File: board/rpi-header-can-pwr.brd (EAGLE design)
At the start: 65 x 56.5 mm, 40 parts, among them U1 MCP2515, X1 RJ45-8L21-S, X2 RJ45-8L21-S

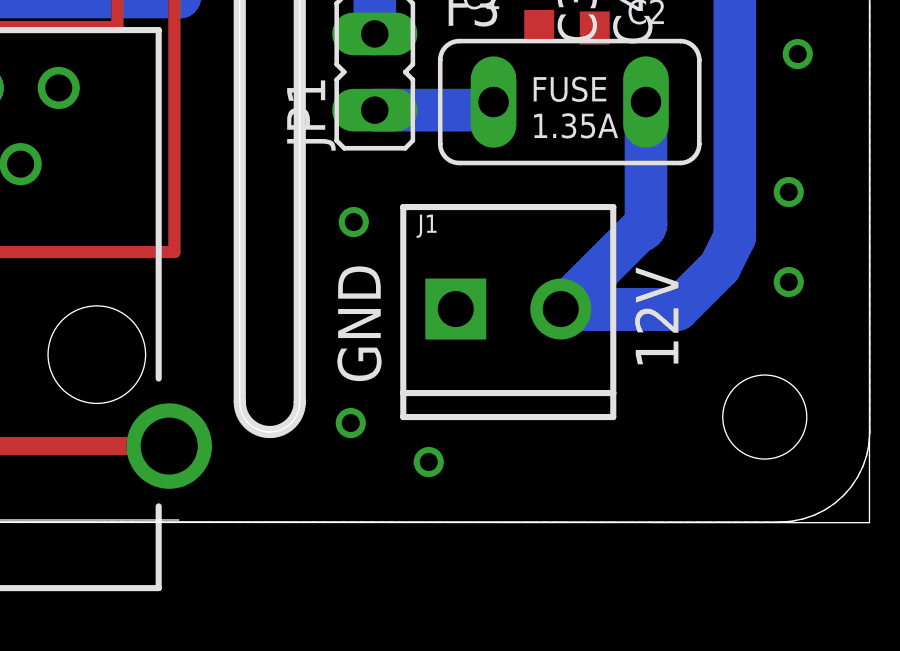
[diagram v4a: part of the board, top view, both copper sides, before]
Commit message: 3.5mm to 5mm screw terminal
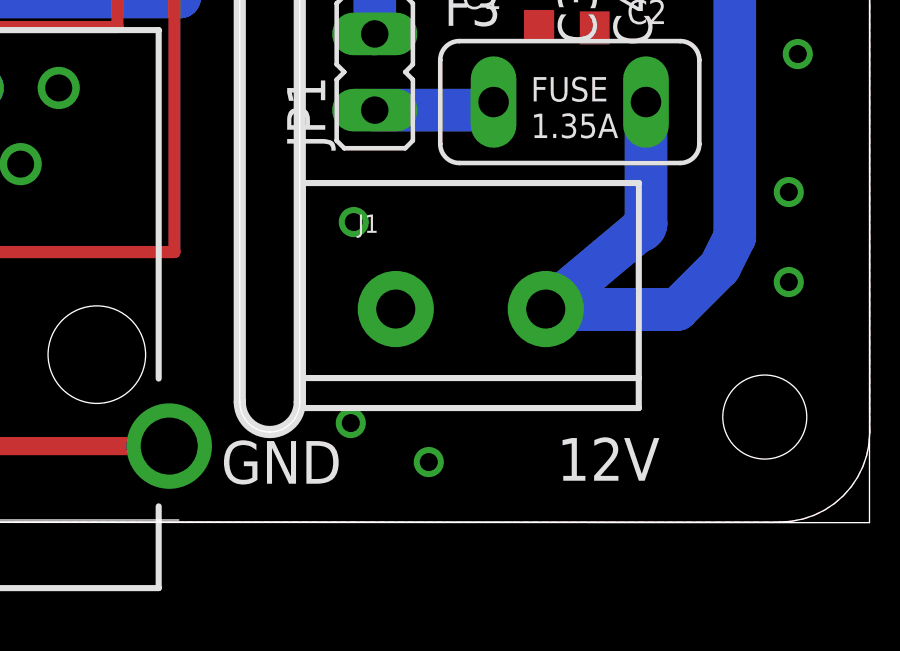
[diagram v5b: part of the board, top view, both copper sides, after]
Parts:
- J1: device SparkFun-Connectors:SCREWTERMINAL-3.5MM-2 -> SparkFun-Connectors:SCREWTERMINAL-5MM-2
- moved J1 2.00 mm to (49.2, 7.10)
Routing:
- net PRE_FUSE_12V: track 42.5 -> 43.4 mm
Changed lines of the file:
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@@
 <text x="6.5" y="43.5" size="1.016" layer="121">FUSE
 2.5A</text>
-<text x="57.2" y="8.5" size="1.4224" layer="121" rot="R270">12V</text>
-<text x="48.7" y="4.6" size="1.4224" layer="121" rot="R90">GND</text>
+<text x="58" y="2.8" size="1.4224" layer="121" rot="R180">12V</text>
+<text x="47.4" y="2.7" size="1.4224" layer="121" rot="R180">GND</text>
 <text x="11.9" y="24.6" size="0.8128" layer="121">D4</text>
 <text x="5.9" y="27.3" size="0.8128" layer="121">R15</text>
@@
 <element name="D3" library="transistor" package="SOT23" value="BC846" x="8" y="38" rot="MR0"/>
 <element name="R4" library="rcl" package="R0603" value="1k" x="8" y="33" rot="MR270"/>
-<element name="J1" library="SparkFun-Connectors" package="SCREWTERMINAL-3.5MM-2" value="" x="51.2" y="7.1">
-<attribute name="PROD_ID" value="CONN-08399" x="51.2" y="7.1" size="1.778" layer="27" display="off"/>
+<element name="J1" library="SparkFun-Connectors" package="SCREWTERMINAL-5MM-2" value="" x="49.2" y="7.1">
+<attribute name="SF_SKU" value="PRT-08432" x="49.2" y="7.1" size="1.778" layer="27" display="off"/>
 </element>
 <element name="GND84" library="SparkFun-Connectors" package="SCREWTERMINAL-3.5MM-2" value="" x="4.5" y="15.5" rot="R270">
@@
 <contactref element="F3" pad="2"/>
 <contactref element="J1" pad="2"/>
-<wire x1="54.7" y1="7.1" x2="54.7" y2="7.085796875" width="1.4224" layer="16"/>
+<wire x1="54.2" y1="7.1" x2="54.7" y2="7.085796875" width="1.4224" layer="16"/>
 <wire x1="57.54" y1="9.94" x2="57.3" y2="9.7" width="1.4224" layer="16"/>
-<wire x1="57.3" y1="9.7" x2="54.7" y2="7.1" width="1.4224" layer="16"/>
+<wire x1="57.3" y1="9.7" x2="54.2" y2="7.1" width="1.4224" layer="16"/>
 <wire x1="54.7" y1="7.085796875" x2="58.585796875" y2="7.085796875" width="1.4224" layer="16"/>
 <wire x1="58.585796875" y1="7.085796875" x2="60" y2="8.5" width="1.4224" layer="16"/>

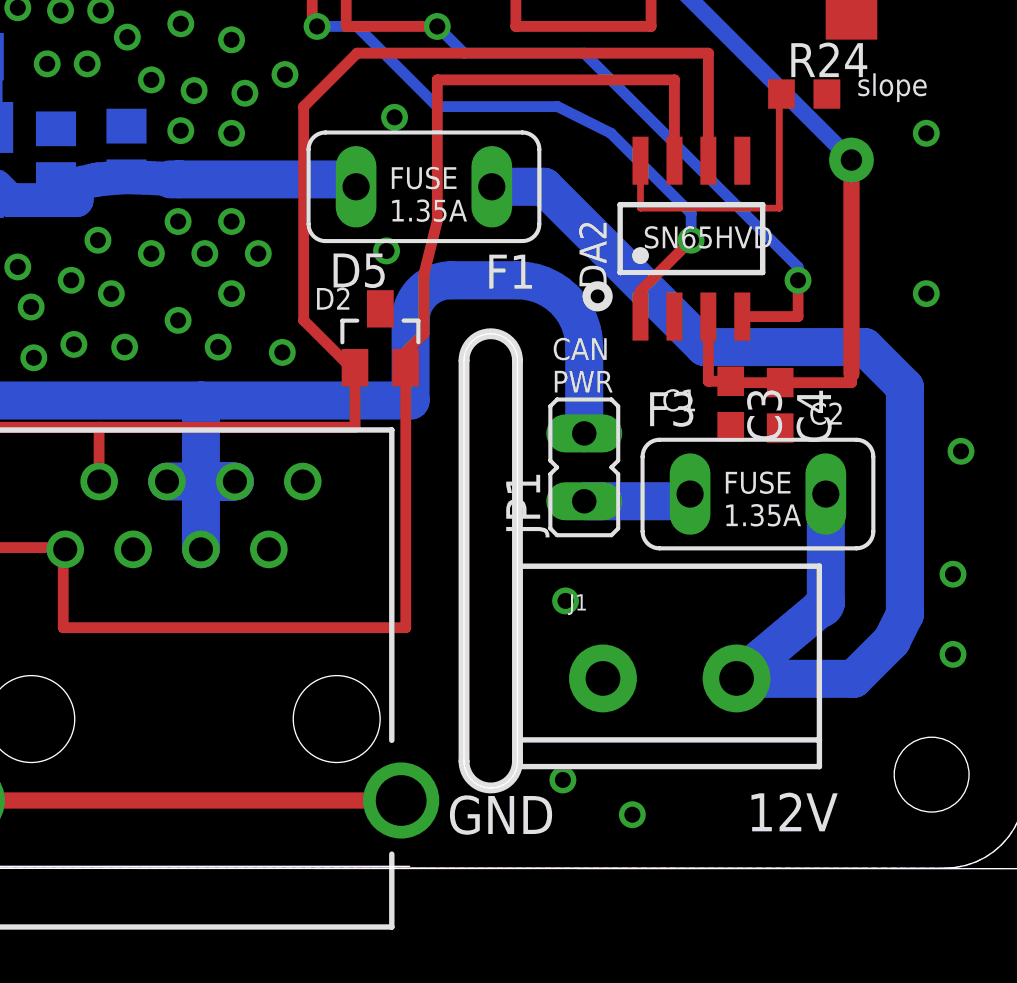
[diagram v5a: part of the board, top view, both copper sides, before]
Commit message: add varistor
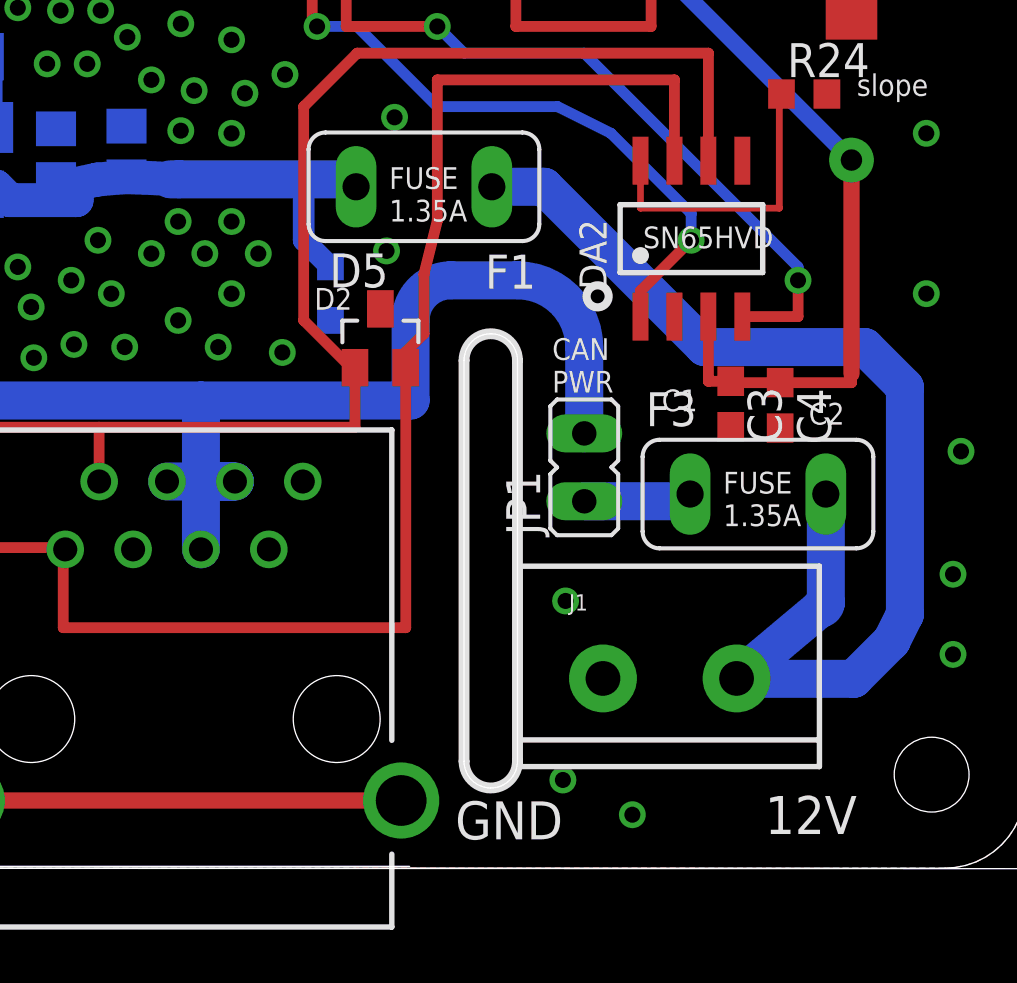
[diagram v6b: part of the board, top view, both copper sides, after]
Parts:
- added R6: VARISTORCN0603, varistor:CT/CN0603
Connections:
- net +12V: now also R6.1
- net GND: now also R6.2
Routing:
- net +12V: track 65.8 -> 69.5 mm
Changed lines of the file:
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@@
 <text x="18.5" y="46.6" size="1.016" layer="122" rot="MR180">C5</text>
 <text x="21.2" y="46.6" size="1.016" layer="122" rot="MR180">C5</text>
-<text x="29.7" y="29" size="1.016" layer="122" rot="MR0">C11</text>
-<text x="32.3" y="28.9" size="1.016" layer="122" rot="MR0">C4</text>
+<text x="29.6" y="28.6" size="1.016" layer="122" rot="MR0">C11</text>
+<text x="31.9" y="28.9" size="1.016" layer="122" rot="MR0">C4</text>
 <circle x="28.4" y="23.6" radius="0.3" width="0.4064" layer="122"/>
 <text x="28.5" y="27.2" size="1.016" layer="122" rot="MR0">ST1S10</text>
 <text x="19.5" y="37" size="0.8128" layer="122" rot="MR0">R18</text>
-<text x="22.5" y="22" size="0.8128" layer="122" rot="MR0">R3</text>
+<text x="21.6" y="21.7" size="0.8128" layer="122" rot="MR0">R3</text>
 <wire x1="5" y1="35" x2="5" y2="20.5" width="0.4064" layer="121"/>
 <wire x1="4" y1="19.5" x2="1.5" y2="19.5" width="0.4064" layer="121"/>
@@
 <text x="6.5" y="43.5" size="1.016" layer="121">FUSE
 2.5A</text>
-<text x="58" y="2.8" size="1.4224" layer="121" rot="R180">12V</text>
-<text x="47.4" y="2.7" size="1.4224" layer="121" rot="R180">GND</text>
+<text x="58.7" y="2.7" size="1.4224" layer="121" rot="R180">12V</text>
+<text x="47.7" y="2.5" size="1.4224" layer="121" rot="R180">GND</text>
 <text x="11.9" y="24.6" size="0.8128" layer="121">D4</text>
 <text x="5.9" y="27.3" size="0.8128" layer="121">R15</text>
@@
 PWR</text>
 <text x="2.8" y="17.9" size="1.016" layer="121">tamper</text>
-<text x="8.5" y="30" size="0.8128" layer="122" rot="MR0">R5</text>
+<text x="7.8" y="30.1" size="0.8128" layer="122" rot="MR0">R5</text>
 <text x="5.8" y="37.9" size="0.8128" layer="122" rot="MR0">T3</text>
 <text x="11.8" y="32.4" size="0.8128" layer="122" rot="MR0">D6</text>
 <text x="53.7" y="12.8" size="0.8128" layer="121">FUSE
 1.35A</text>
+<text x="38" y="20.8" size="0.8128" layer="122" rot="MR0">D6</text>
 </plain>
 <attributes>
@@
 <attribute name="MPN" value="" x="55" y="14" size="1.778" layer="27" display="off"/>
 </element>
+<element name="R6" library="varistor" package="CT/CN0603" value="VARISTORCN0603" x="39" y="21.5" rot="MR270"/>
 </elements>
 <signals>
@@
 <via x="33.3" y="24.2" extent="1-16" drill="0.6"/>
 <via x="41.1" y="23.1" extent="1-16" drill="0.6"/>
+<contactref element="R6" pad="2"/>
 </signal>
 <signal name="CAN_TX">
@@
 <wire x1="25.275" y1="25.22" x2="26" y2="25.5" width="0.6096" layer="16"/>
 <wire x1="33.34531875" y1="25.778828125" x2="33" y2="25.778828125" width="1.4224" layer="16"/>
-<wire x1="33.34531875" y1="25.778828125" x2="39.681171875" y2="25.778828125" width="1.4224" layer="16"/>
+<wire x1="33.34531875" y1="25.778828125" x2="38" y2="25.778828125" width="1.4224" layer="16"/>
 <contactref element="F1" pad="2"/>
+<wire x1="38" y1="25.778828125" x2="39.681171875" y2="25.778828125" width="1.4224" layer="16"/>
 <wire x1="39.96" y1="25.5" x2="39.681171875" y2="25.778828125" width="1.4224" layer="16"/>
+<contactref element="R6" pad="1"/>
+<wire x1="39" y1="22.5" x2="38" y2="23.5" width="0.8128" layer="16"/>
+<wire x1="38" y1="23.5" x2="38" y2="25.778828125" width="0.8128" layer="16"/>
 </signal>
 <signal name="N$1">

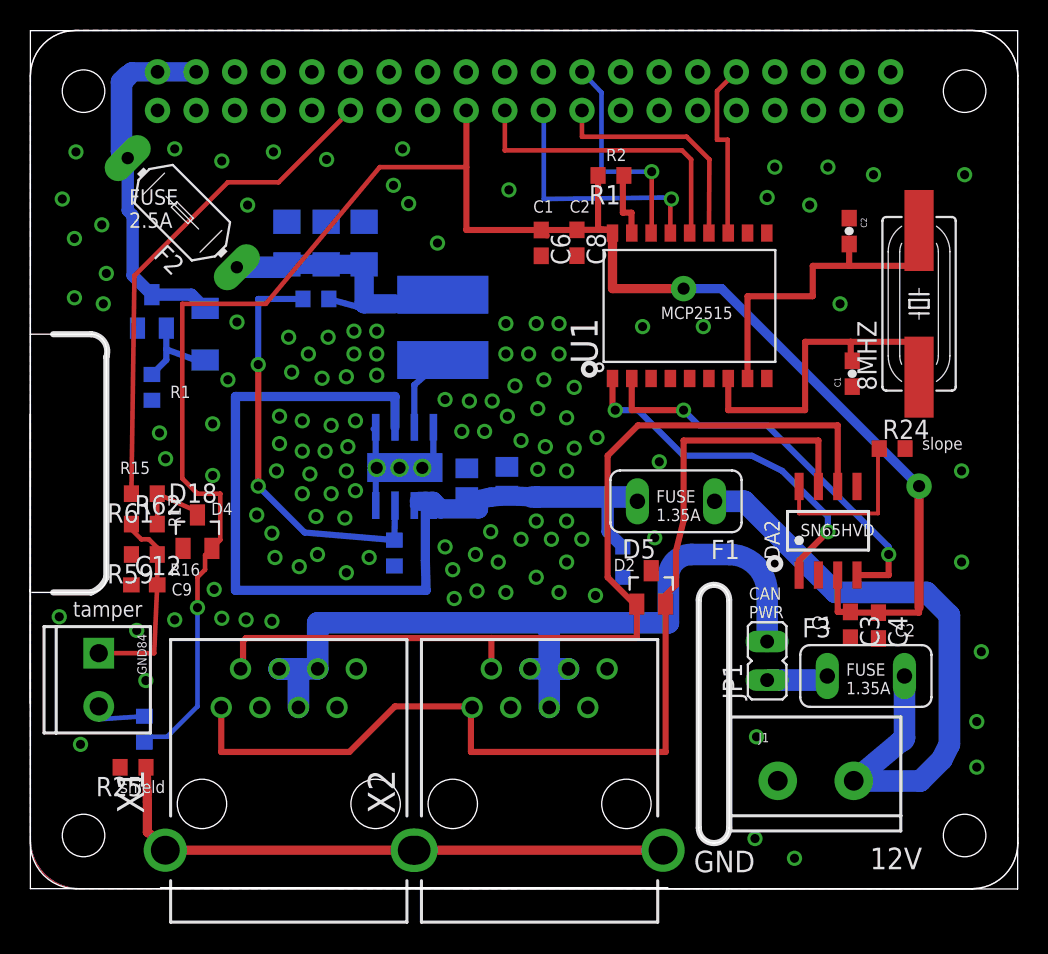
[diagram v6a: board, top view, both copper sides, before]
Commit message: add holes for rpi zero
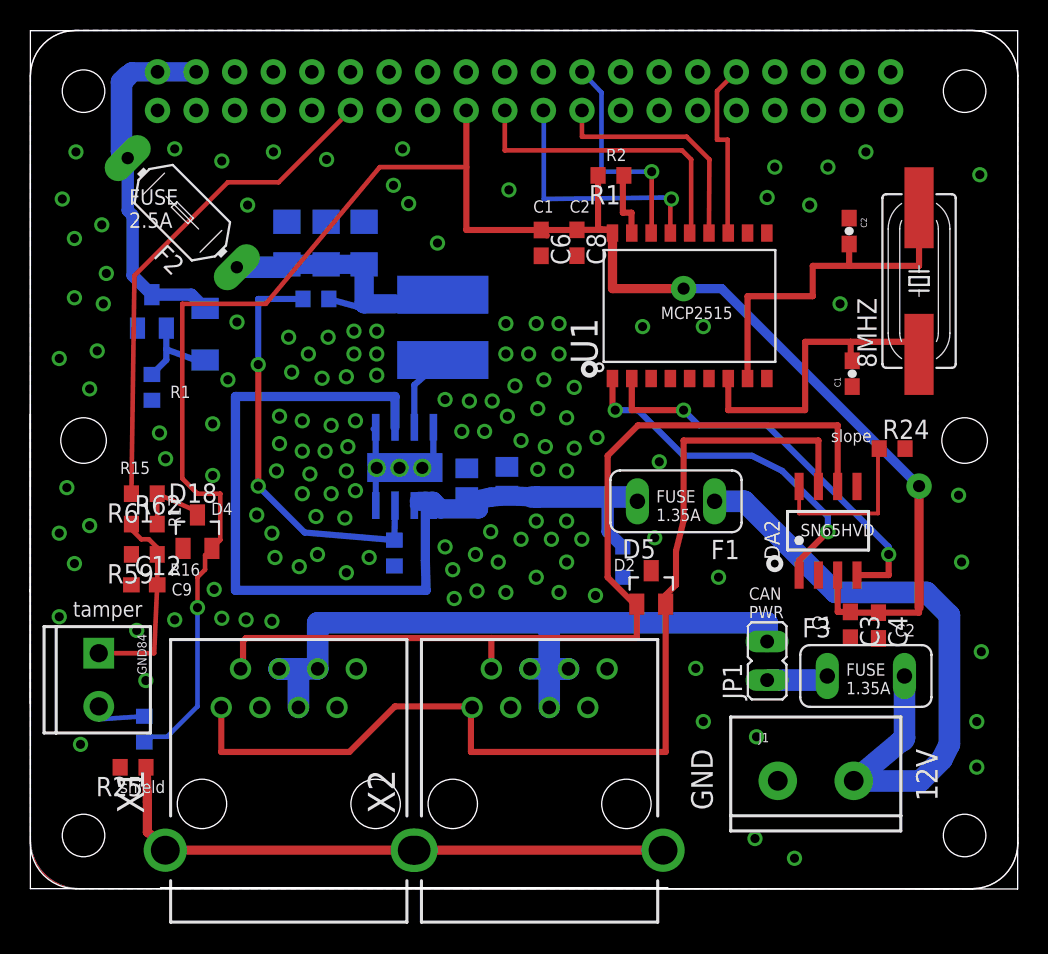
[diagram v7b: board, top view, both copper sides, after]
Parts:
- RPI1: value RASPBERRYPI_BPLUS_HATSLOTS -> RASPBERRYPI_BPLUS_HATNOSLOTS; device microbuilder:PI_HAT_SLOTS -> microbuilder:PI_HAT_NOSLOTS
- moved 8MHZ 1.50 mm to (58.5, 40.0)
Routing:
- net RJ45_12V: track 56.2 -> 49.6 mm
- net N$3: track 22.8 -> 21.3 mm
- net N$2: track 22.5 -> 24.0 mm
- net GND: vias 128 -> 138
